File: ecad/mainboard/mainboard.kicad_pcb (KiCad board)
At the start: 2 copper layers, 100.2 x 76 mm, 27 parts, among them J1 ESP32C3 Super Mini Left, J2 ESP32C3 Super Mini Right, J5 Dot Matrix Side A, J6 Dot Matrix Side B, SW1 Left Button, SW2 Right Button, U1 PCF8575DBR

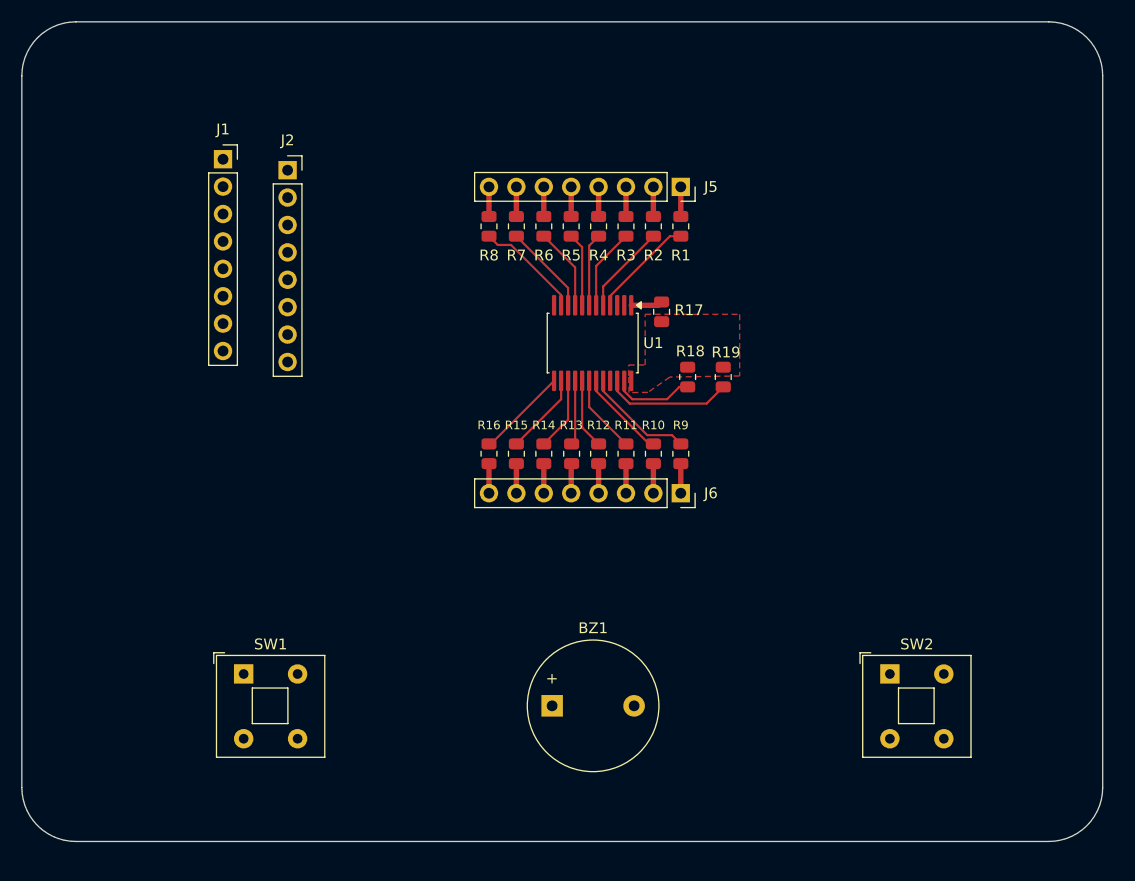
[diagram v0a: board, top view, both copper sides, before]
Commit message: resize and reposition edge cuts
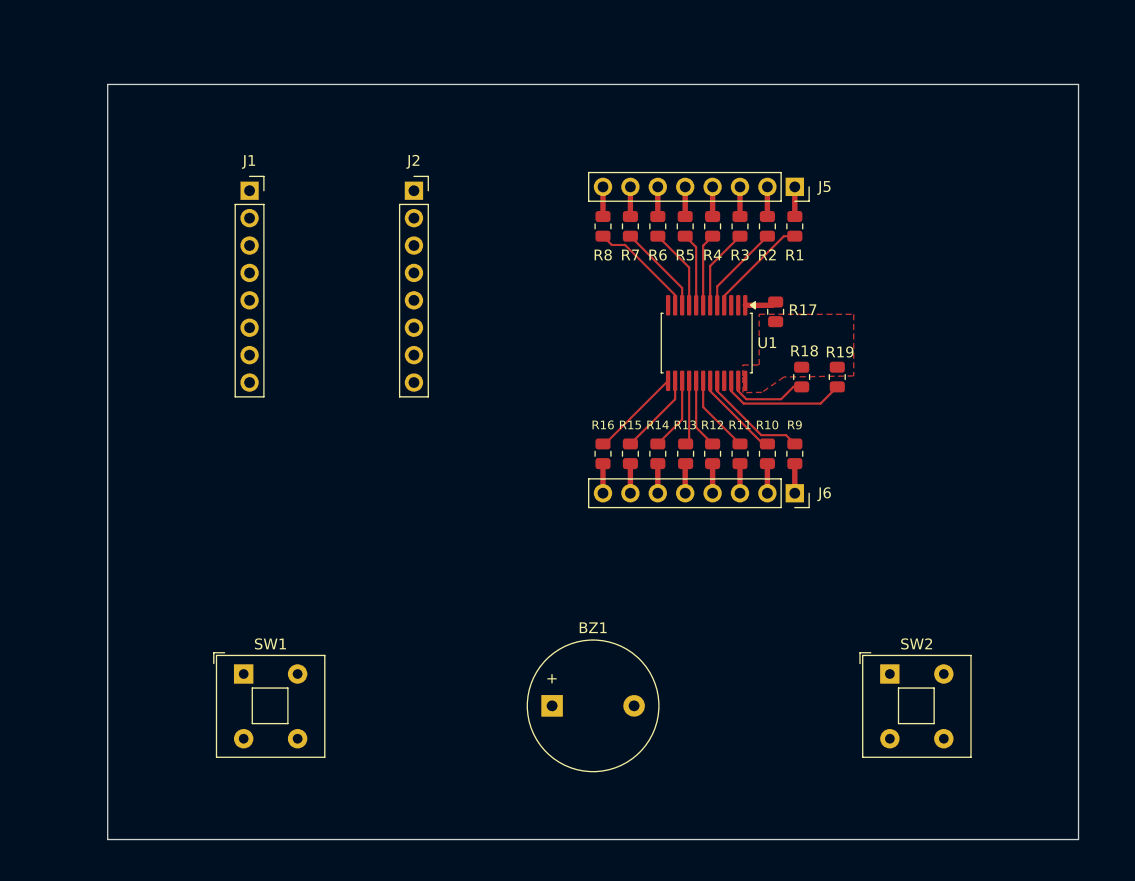
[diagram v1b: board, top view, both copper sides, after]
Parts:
- moved J2 11.9 mm to (106.8, 72.1)
- moved J5 10.6 mm to (142.1, 71.8)
- moved J6 10.6 mm to (142.1, 100.2)
- moved R1 10.6 mm to (142.1, 75.4)
- moved R12 10.6 mm to (134.5, 96.5)
- moved R13 10.6 mm to (132.0, 96.5)
- moved R15 10.6 mm to (126.9, 96.5)
- moved R18 10.6 mm to (142.8, 89.4)
- moved R19 10.6 mm to (146.1, 89.4)
- moved R4 10.6 mm to (134.5, 75.4)
- moved R5 10.6 mm to (132.0, 75.4)
- moved R7 10.6 mm to (126.9, 75.4)
- moved R9 10.6 mm to (142.1, 96.5)
- moved R11 10.6 mm to (137.1, 96.5)
- moved R14 10.6 mm to (129.4, 96.5)
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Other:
- board size 100.2 x 76 mm -> 90 x 70 mm

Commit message: route all components and pass drc
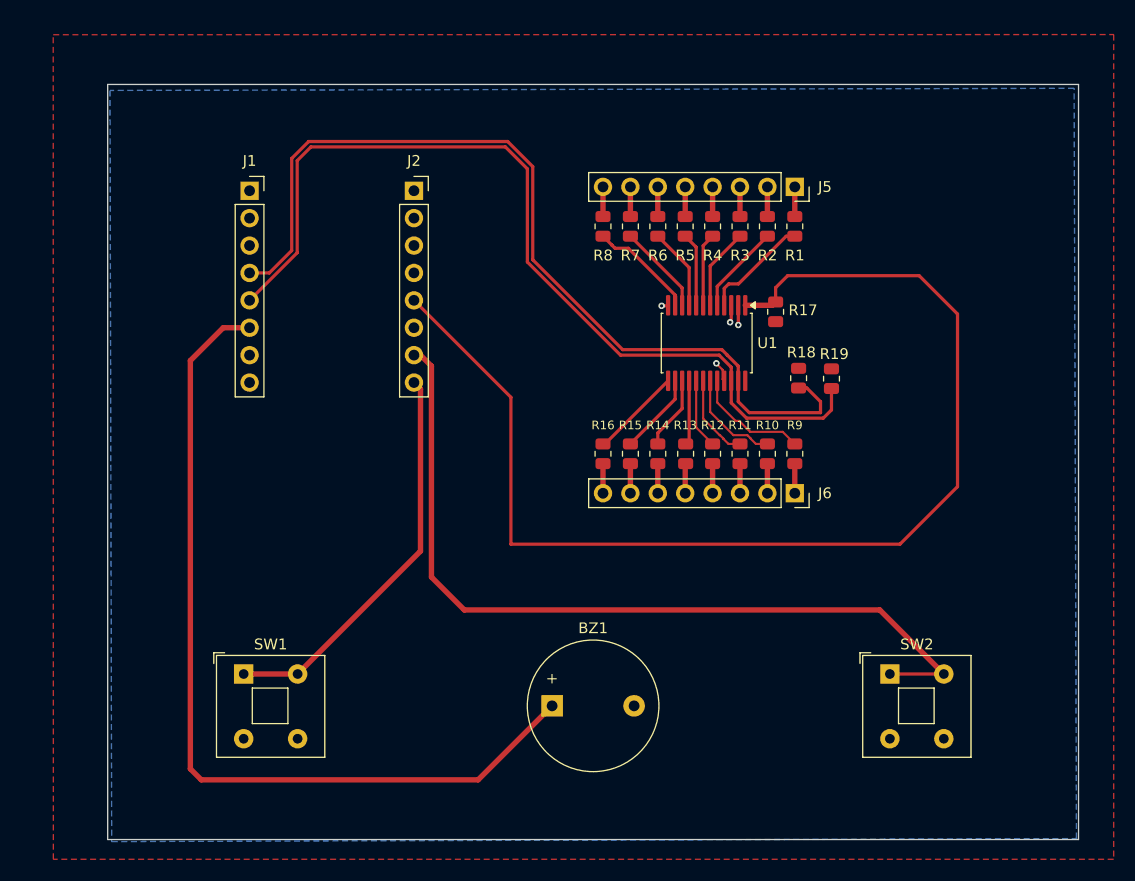
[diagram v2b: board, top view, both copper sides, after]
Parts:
- moved R19 0.56 mm to (145.5, 89.6)
- moved R18 0.30 mm to (142.5, 89.5)
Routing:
- net /~{INT}: track 2.94 -> 109.0 mm
- net /BUZZ: track 0.00 -> 81.4 mm
- net /RIGHT_BTN: track 0.00 -> 77.8 mm
- net /SDA: track 7.62 -> 84.0 mm
- net /SCL: track 11.9 -> 84.5 mm
- net /LEFT_BTN: track 0.00 -> 37.0 mm
- net GND: track 0.00 -> 6.02 mm, vias 0 -> 4
- net /P16: track 8.28 -> 9.43 mm
- net /P15: track 7.27 -> 7.91 mm
- net /P17: track 10.2 -> 10.8 mm
- added copper zone on B.Cu, net GND

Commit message: add text to back silkscreen and mounting holes
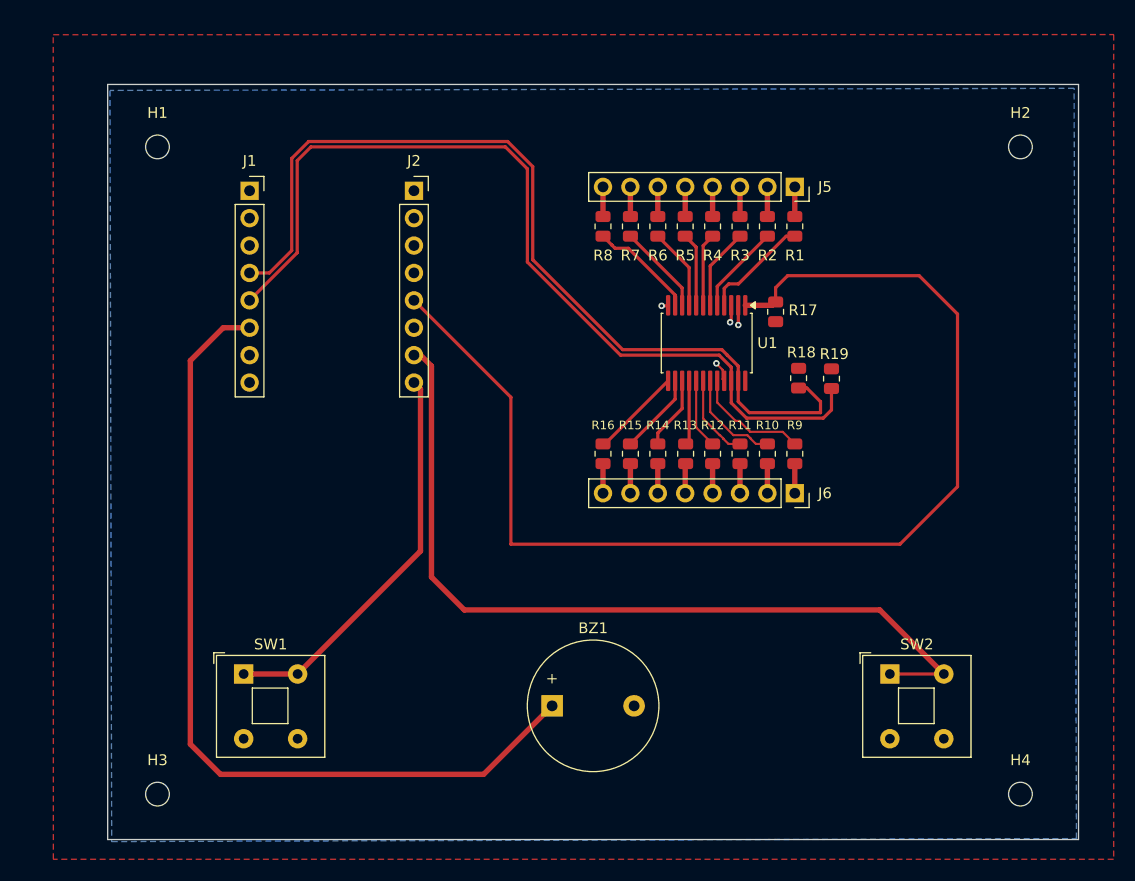
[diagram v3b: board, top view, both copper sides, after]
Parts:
- added H1: MountingHole, MountingHole:MountingHole_2.2mm_M2, F.Cu at (83.1, 68.1)
- added H2: MountingHole, MountingHole:MountingHole_2.2mm_M2, F.Cu at (163.1, 68.1)
- added H3: MountingHole, MountingHole:MountingHole_2.2mm_M2, F.Cu at (83.1, 128.1)
- added H4: MountingHole, MountingHole:MountingHole_2.2mm_M2, F.Cu at (163.1, 128.1)
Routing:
- net /BUZZ: track 81.4 -> 79.6 mm
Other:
- board text added: "{dblquote}SnakeGame{dblquote} Board V1 Designed by Ibukun Ekunwe (drvnprgrmr)"
